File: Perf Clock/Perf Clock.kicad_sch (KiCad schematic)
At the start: 7 parts, among them U1 PIC16LF1826IP, U2 74HC595, U3 74HC595, U4 TLC5916IN, U5 TLC5916IN

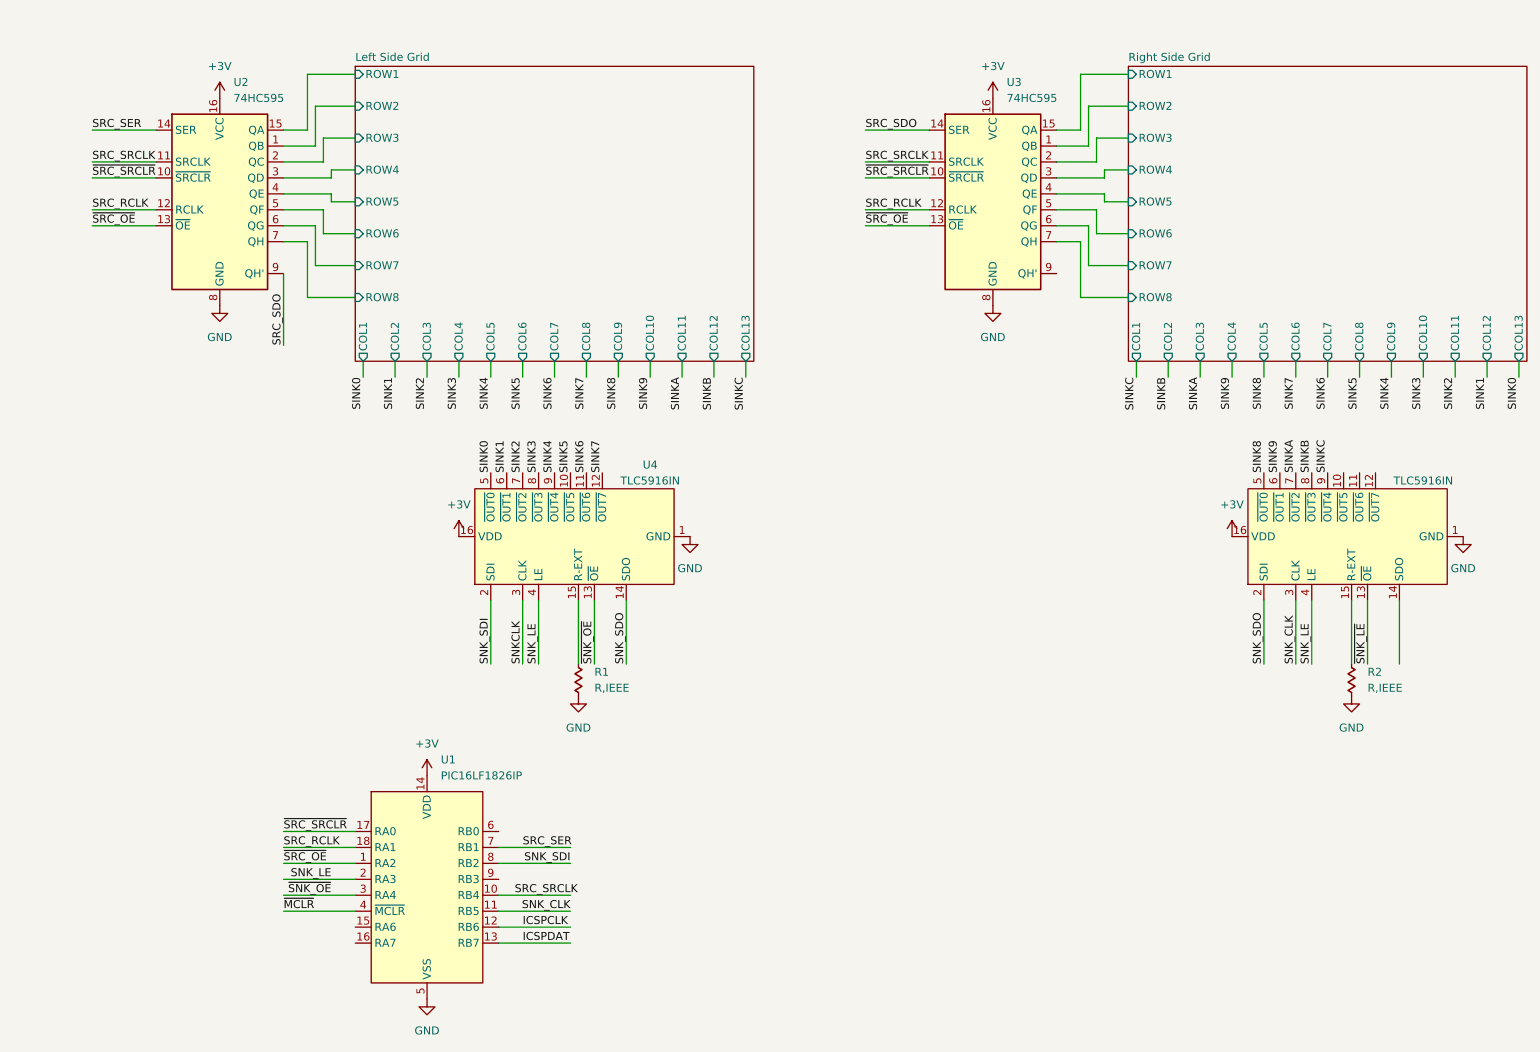
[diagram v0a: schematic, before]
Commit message: Updated KiCad Schematic
Updated KiCad Schematic and made a pdf of it.
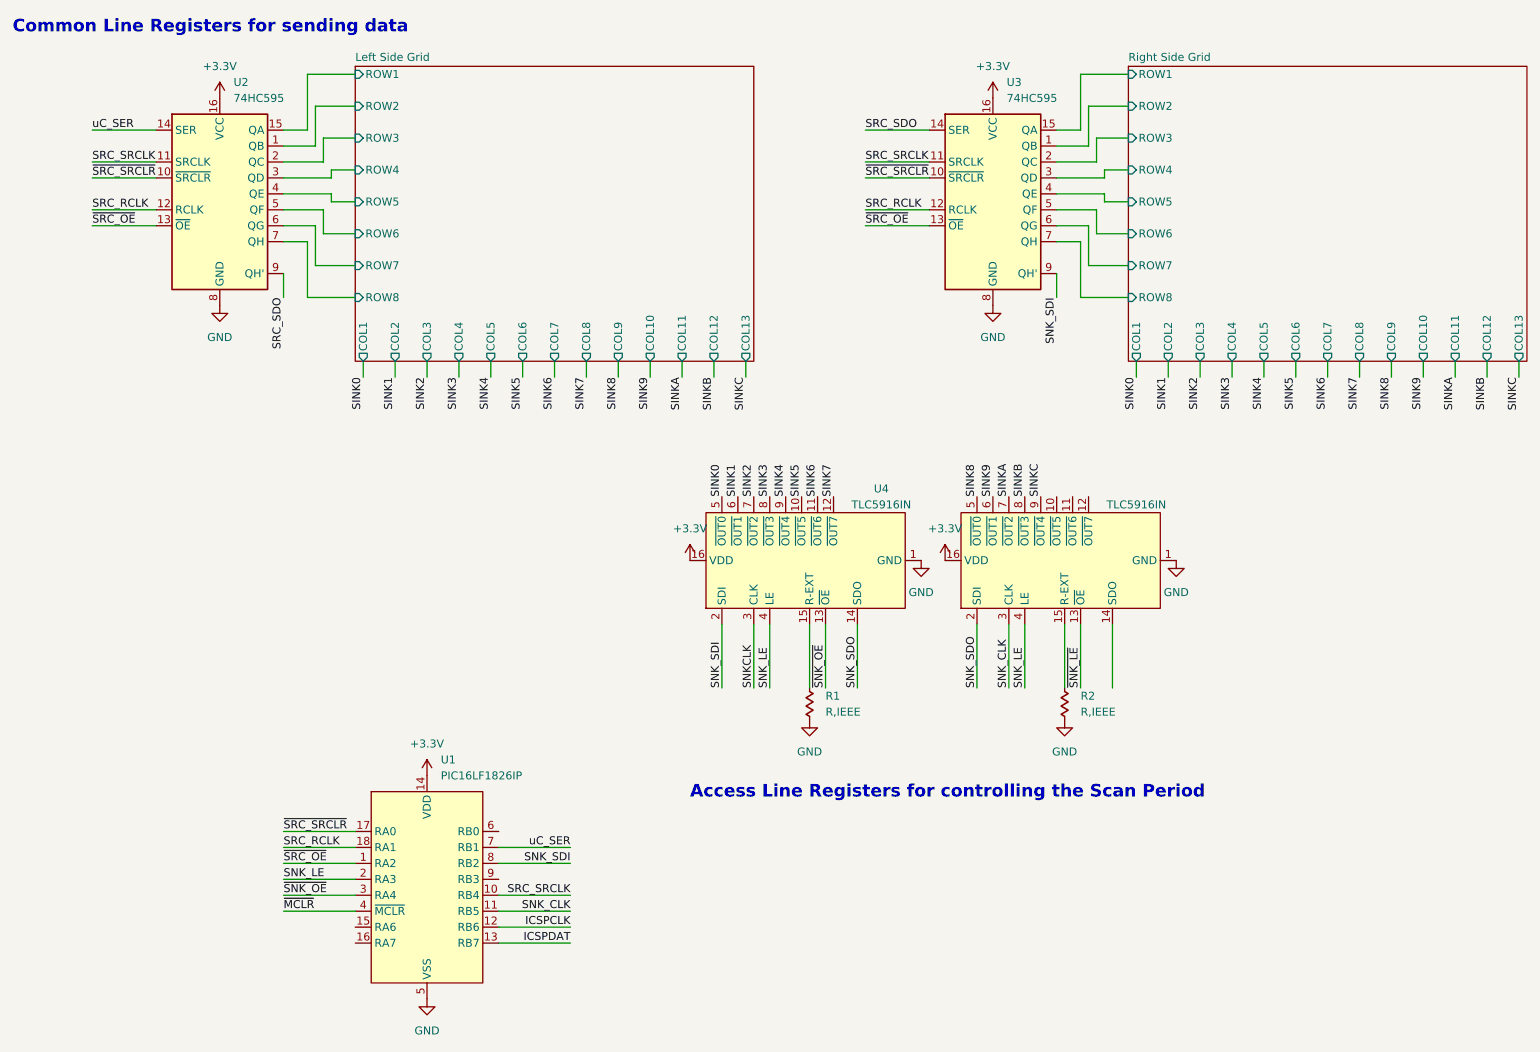
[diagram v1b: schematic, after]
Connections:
- net SNK_SDI: now also U3.9 (QH')
- net SRC_SER renamed uC_SER
- net VDD renamed +3.3V
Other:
- note added: "Access Line Registers for controlling the Scan Period"
- note added: "Common Line Registers for sending data"
- moved on the sheet: R1, R2, U4
